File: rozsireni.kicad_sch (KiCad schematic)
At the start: 10 parts, among them J12 GPIO rezerva

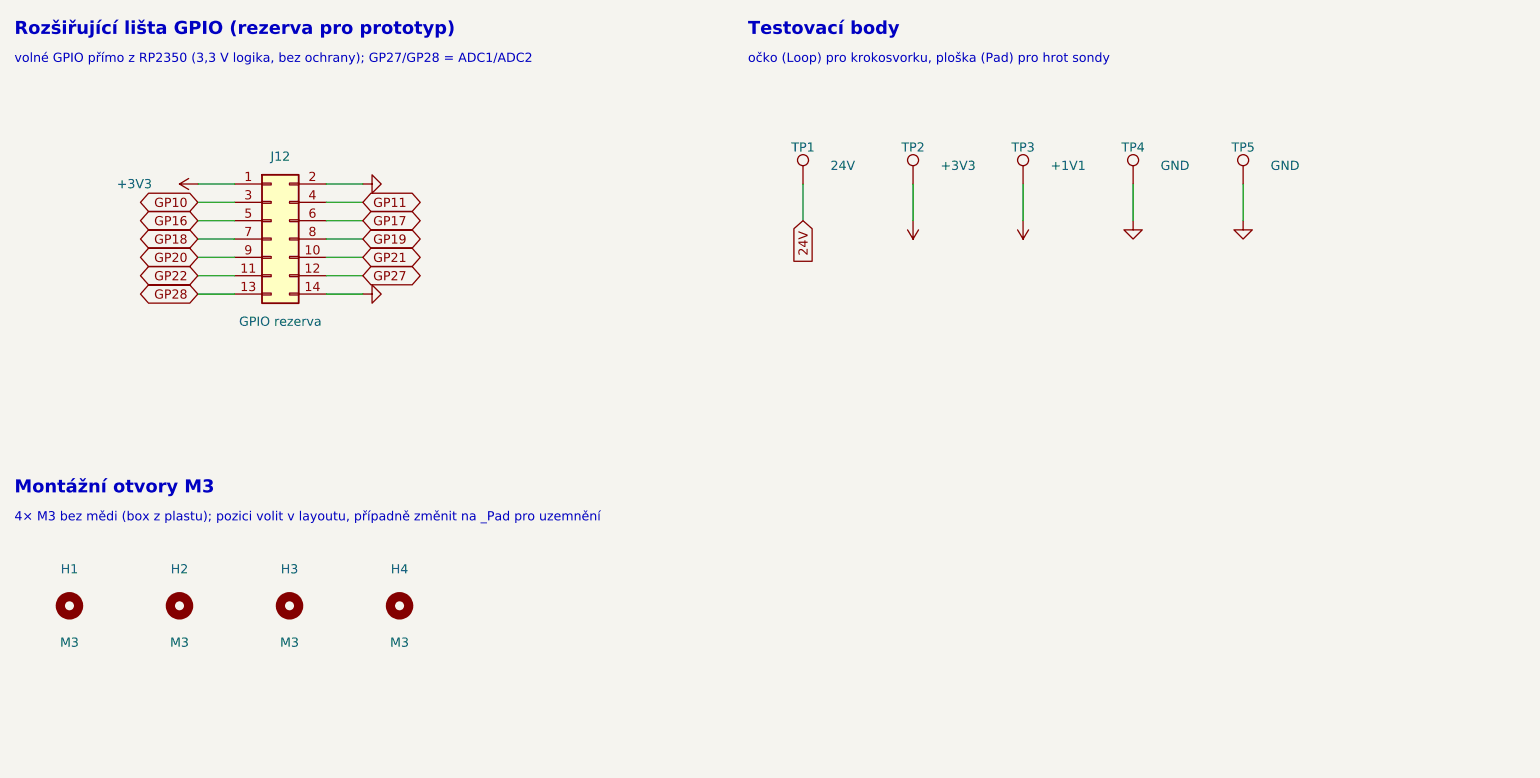
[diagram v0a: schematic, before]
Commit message: Add communication test points, tidy root sheet, board setup
- Test points TP6-TP19 (1 mm pads) on I2C1, I2C0, HX711, RM2 gSPI,
  heater/fan/exhaust PWM and NTC ADC, plus TP12 GND loop
- Root sheet: GPIO2-5 -> J6/J7 and GPIO24/25/29 -> RM2 now connected by
  global labels (HX711_DT/SCK, WL_DATA/CS/CLK), J6 moved
- Board updated from schematic (F8)
- Board setup: min through-hole 0.2 mm (0.25 mm vias under RP2350),
  new net class Power (1.5 mm track, 0.3 mm clearance, 0.8/0.4 via)
  for 24V_IN, 24V, fuse/heater nets

Co-Authored-By: Claude Opus 5.5 <noreply@anthropic.com>
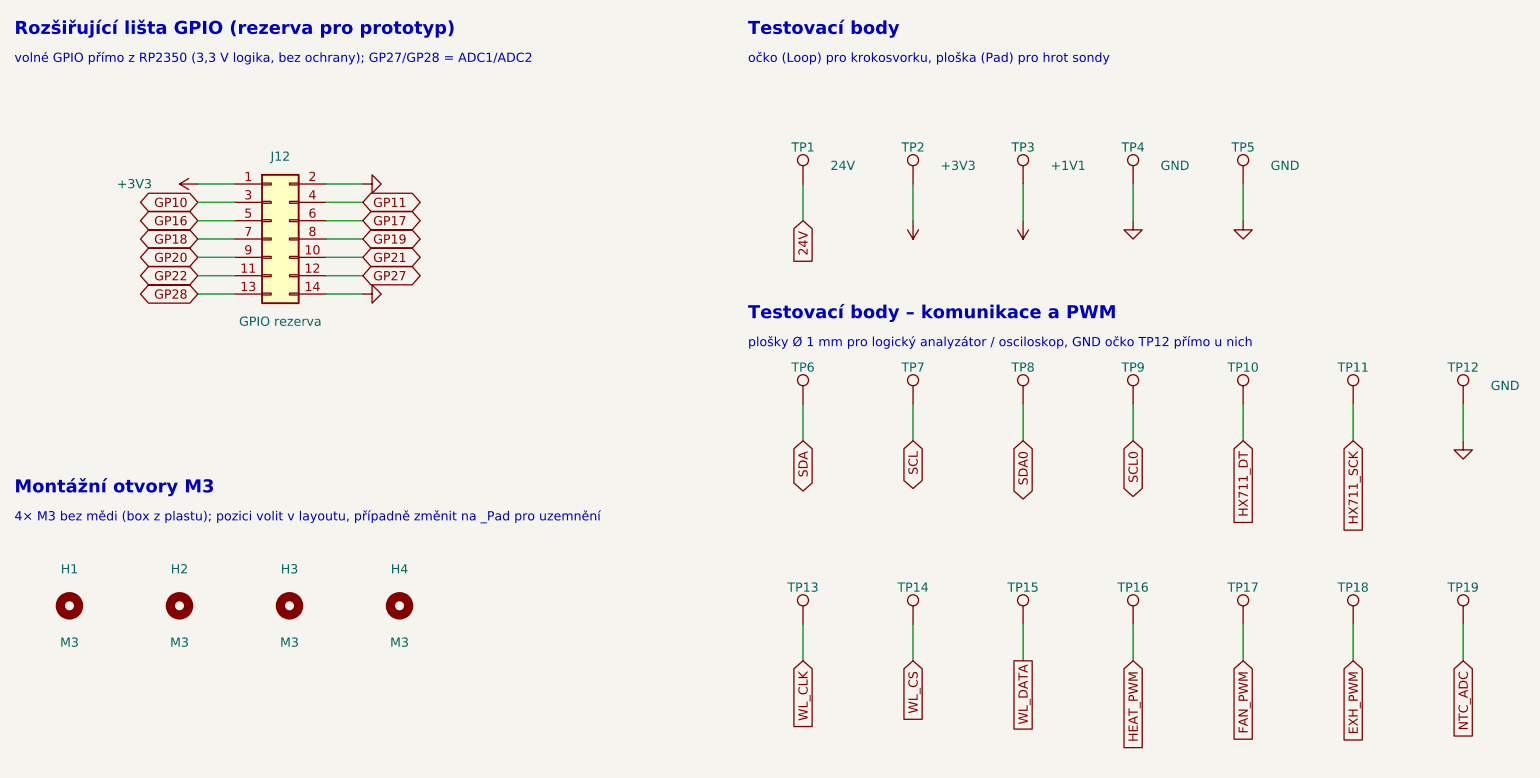
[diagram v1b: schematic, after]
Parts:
- added TP10: HX711_DT, TestPoint:TestPoint_Pad_D1.0mm, symbol Connector:TestPoint
- added TP11: HX711_SCK, TestPoint:TestPoint_Pad_D1.0mm, symbol Connector:TestPoint
- added TP12: GND, TestPoint:TestPoint_Loop_D2.50mm_Drill1.0mm, symbol Connector:TestPoint
- added TP13: WL_CLK, TestPoint:TestPoint_Pad_D1.0mm, symbol Connector:TestPoint
- added TP14: WL_CS, TestPoint:TestPoint_Pad_D1.0mm, symbol Connector:TestPoint
- added TP15: WL_DATA, TestPoint:TestPoint_Pad_D1.0mm, symbol Connector:TestPoint
- added TP16: HEAT_PWM, TestPoint:TestPoint_Pad_D1.0mm, symbol Connector:TestPoint
- added TP17: FAN_PWM, TestPoint:TestPoint_Pad_D1.0mm, symbol Connector:TestPoint
- added TP18: EXH_PWM, TestPoint:TestPoint_Pad_D1.0mm, symbol Connector:TestPoint
- added TP19: NTC_ADC, TestPoint:TestPoint_Pad_D1.0mm, symbol Connector:TestPoint
- added TP6: SDA, TestPoint:TestPoint_Pad_D1.0mm, symbol Connector:TestPoint
- added TP7: SCL, TestPoint:TestPoint_Pad_D1.0mm, symbol Connector:TestPoint
- added TP8: SDA0, TestPoint:TestPoint_Pad_D1.0mm, symbol Connector:TestPoint
- added TP9: SCL0, TestPoint:TestPoint_Pad_D1.0mm, symbol Connector:TestPoint
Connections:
- net GND: now also TP12.1
- new net EXH_PWM: TP18.1
- new net FAN_PWM: TP17.1
- new net HEAT_PWM: TP16.1
- new net HX711_DT: TP10.1
- new net HX711_SCK: TP11.1
- new net NTC_ADC: TP19.1
- new net SCL: TP7.1
- new net SCL0: TP9.1
- new net SDA: TP6.1
- new net SDA0: TP8.1
- new net WL_CLK: TP13.1
- new net WL_CS: TP14.1
- new net WL_DATA: TP15.1
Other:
- note added: "Testovací body – komunikace a PWM"
- note added: "plošky Ø 1 mm pro logický analyzátor / osciloskop, GND očko TP12 přímo u nich"

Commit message: Layout review fixes and JLCPCB fabrication outputs
- In2: GND pour over the whole board (priority 0) below the 3V3 zones
- Silkscreen: +/- marks of J5, J8, J9 moved out from under the terminal
  blocks; D4 and TP13 labels moved to visible spots
- TP12 moved away from the RM2 antenna keep-out, J4 shifted up,
  R20 220R so the D6 LED is visible at 3.3 V
- NTC (J10, R25, C26, TP19) excluded from this prototype board
- gerber/: fresh Gerber + Excellon export, JLCPCB zip, ordering notes
- CLAUDE.md, .claude/pamet.md: review results and decisions

Co-Authored-By: Claude Opus 5.5 <noreply@anthropic.com>
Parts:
- TP19: now not fitted
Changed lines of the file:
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@@
 		(exclude_from_sim no)
 		(in_bom yes)
-		(on_board yes)
-		(dnp no)
+		(on_board no)
+		(dnp yes)
 		(property "Reference" "TP19"
 			(at 226.06 111.76 0)
